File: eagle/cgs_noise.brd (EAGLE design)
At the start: 100 x 80 mm, 42 parts, among them IC2 LM3900N, Q1 2N3906, Q2 2N3906

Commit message: routed
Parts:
- moved C9 33.9 mm to (17.8, 54.6), turned to 0 degrees
- moved R17 25.0 mm to (67.3, 38.1)
- moved C2 7.43 mm to (52.7, 61.0)
- moved C8 6.48 mm to (48.3, 24.1), turned to 0 degrees
- moved R7 6.38 mm to (35.6, 59.1), turned to 180 degrees
- moved R10 5.85 mm to (31.1, 53.3), turned to 180 degrees
- moved C15 4.02 mm to (67.3, 22.9), turned to 0 degrees
- moved R1 3.81 mm to (35.6, 63.5)
- moved R9 3.59 mm to (67.3, 35.6)
- moved Q2 2.84 mm to (44.5, 61.0)
- moved R12 2.84 mm to (41.9, 33.0), turned to 180 degrees
- moved C13 2.62 mm to (48.9, 29.2)
- moved C6 2.54 mm to (58.4, 21.6)
- moved R4 2.54 mm to (62.2, 27.9)
- moved R3 2.01 mm to (33.7, 27.3)
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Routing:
- net GND: track 382.4 -> 325.7 mm
- net -12V: track 98.3 -> 47.3 mm
- net N$4: track 28.1 -> 66.8 mm, vias 0 -> 2
- net +12V: track 192.0 -> 165.7 mm
- net N$22: track 49.1 -> 24.6 mm
- net N$1: track 40.3 -> 16.0 mm
- net N$5: track 109.8 -> 129.8 mm, vias 2 -> 0
- net N$2: track 18.7 -> 5.82 mm
- net N$23: track 41.2 -> 32.1 mm
- net N$6: track 3.86 -> 11.3 mm
- net N$51: track 106.0 -> 101.8 mm
- net N$16: track 17.9 -> 13.8 mm
- net N$12: track 57.7 -> 61.6 mm
- net N$17: track 7.62 -> 3.86 mm
- net N$15: track 22.2 -> 18.6 mm
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
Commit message: gcode
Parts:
- moved PWR1 48.2 mm to (55.2, 58.4), turned to 270 degrees
- moved U$3 43.1 mm to (46.4, 67.9), turned to 180 degrees
- moved U$2 40.7 mm to (49.5, 40.6), turned to 180 degrees
- moved C6 33.0 mm to (25.4, 22.2)
- moved C7 31.9 mm to (45.1, 63.5), turned to 180 degrees
- moved C9 30.6 mm to (48.3, 57.8), turned to 90 degrees
- moved R9 26.7 mm to (43.8, 22.9), turned to 90 degrees
- moved C5 22.2 mm to (40.0, 59.1), turned to 90 degrees
- moved R4 21.6 mm to (40.6, 27.3)
- moved BIPOLAR 20.3 mm to (54.6, 0.00)
- moved C2 19.1 mm to (33.7, 61.6), turned to 90 degrees
- moved R15 18.5 mm to (43.8, 47.6)
- moved R11 18.4 mm to (29.8, 36.2)
- moved R18 18.4 mm to (15.9, 19.1)
- moved R17 17.9 mm to (50.2, 33.0), turned to 270 degrees
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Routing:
- net -12V: track 47.3 -> 100.2 mm
- net +12V: track 165.7 -> 128.7 mm
- net N$51: track 101.8 -> 65.6 mm
- net N$5: track 129.8 -> 111.6 mm
- net N$4: track 66.8 -> 50.8 mm
- net GND: track 325.7 -> 310.0 mm
- net N$22: track 24.6 -> 13.1 mm
- net N$18: track 16.0 -> 8.87 mm
- net N$16: track 13.8 -> 9.59 mm
- net N$21: track 12.1 -> 9.83 mm
- net N$12: track 61.6 -> 59.6 mm
- net N$14: track 8.35 -> 9.68 mm
- net N$17: track 3.86 -> 2.54 mm
- net N$13: track 6.35 -> 5.08 mm
- net N$11: track 17.3 -> 18.5 mm
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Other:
- board size 100 x 80 mm -> 100.8 x 80.9 mm

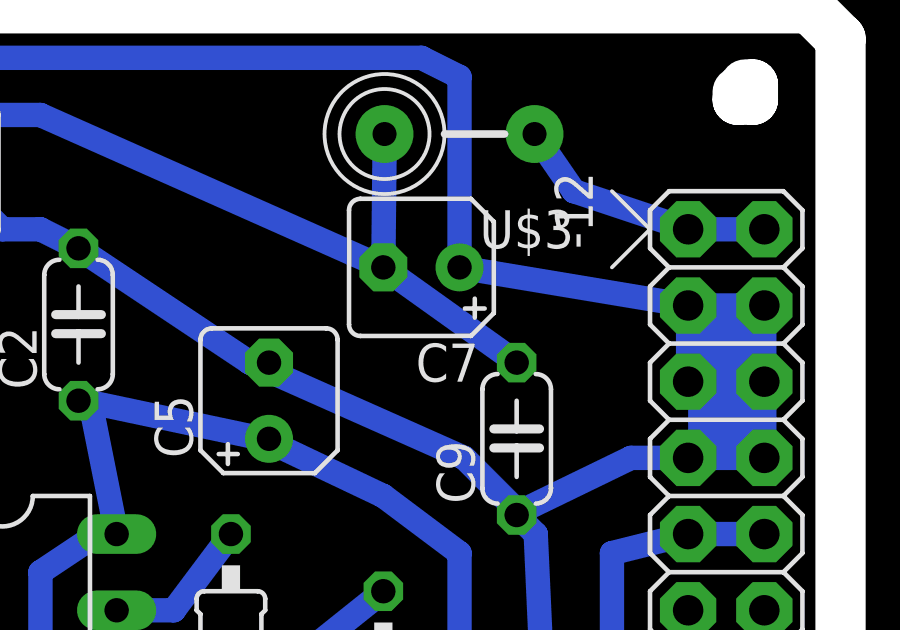
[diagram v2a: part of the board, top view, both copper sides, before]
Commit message: fixed shorted bypass cap trace
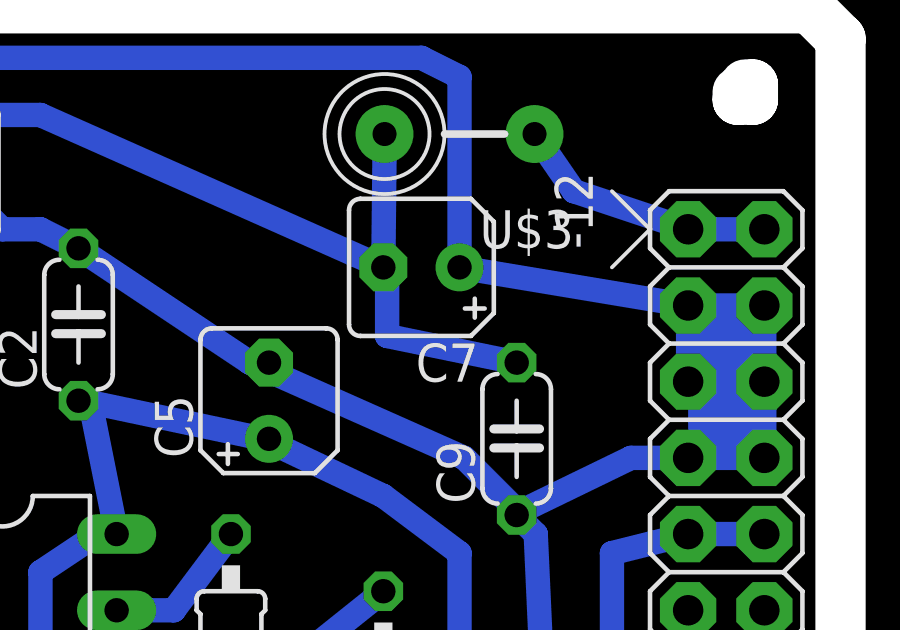
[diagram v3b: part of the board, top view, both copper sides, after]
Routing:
- net -12V: track 100.2 -> 101.6 mm
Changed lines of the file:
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@@
 <wire x1="43.855" y1="67.945" x2="43.855" y2="67.27" width="0.8128" layer="16"/>
 <wire x1="43.855" y1="67.27" x2="43.815" y2="63.5" width="0.8128" layer="16"/>
-<wire x1="43.815" y1="63.5" x2="48.26" y2="60.325" width="0.8128" layer="16"/>
+<wire x1="43.815" y1="63.5" x2="43.942" y2="63.5" width="0.8128" layer="16"/>
+<wire x1="43.942" y1="63.5" x2="43.942" y2="61.214" width="0.8128" layer="16"/>
+<wire x1="43.942" y1="61.214" x2="48.26" y2="60.325" width="0.8128" layer="16"/>
 <wire x1="32.385" y1="68.58" x2="15.875" y2="68.58" width="0.8128" layer="16"/>
 <wire x1="15.875" y1="68.58" x2="2.54" y2="55.245" width="0.8128" layer="16"/>
